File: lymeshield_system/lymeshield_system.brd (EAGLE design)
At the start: 67.9 x 49.5 mm, 56 parts, among them J1 TSW-106-16-L-S-RA, J2 M04B, J3 TSW-103-07-G-D-LL, J4 1844210, U1 MCP79410-I_SN, U2 ATMEGA1608-MU, U3 MX25V1635FM1I, U4 OPA2349EA, U5 DRV8838DSGR, U6 DRV5057A2QDBZ, U7 STLQ015M33R, Y1 ECS-.327-9-1210-TR, Y2 ECS-.327-9-1210-TR

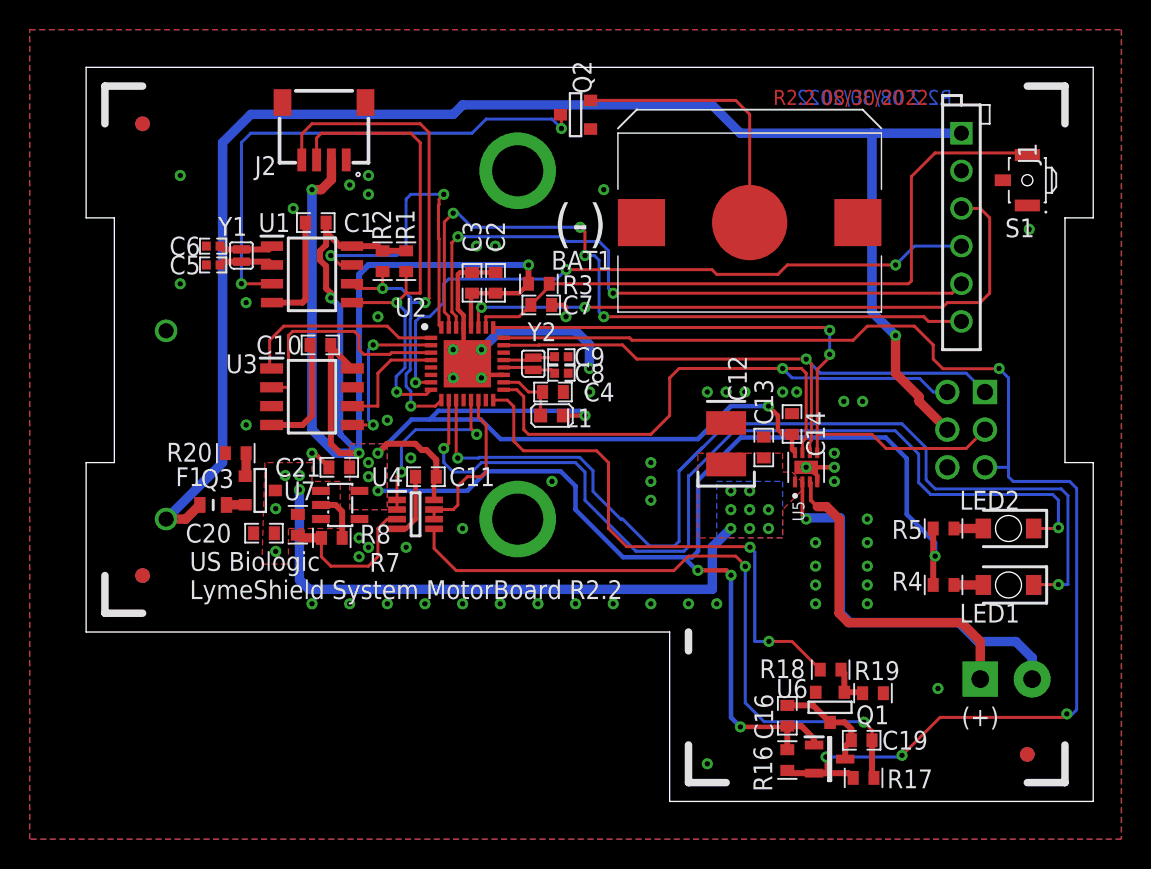
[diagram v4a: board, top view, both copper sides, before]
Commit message: fix (schematics/layout): update for 2.3.a build - Add variant "A" to schematics - Modify footprints for polarization - Update silkscreen for 2.3.a
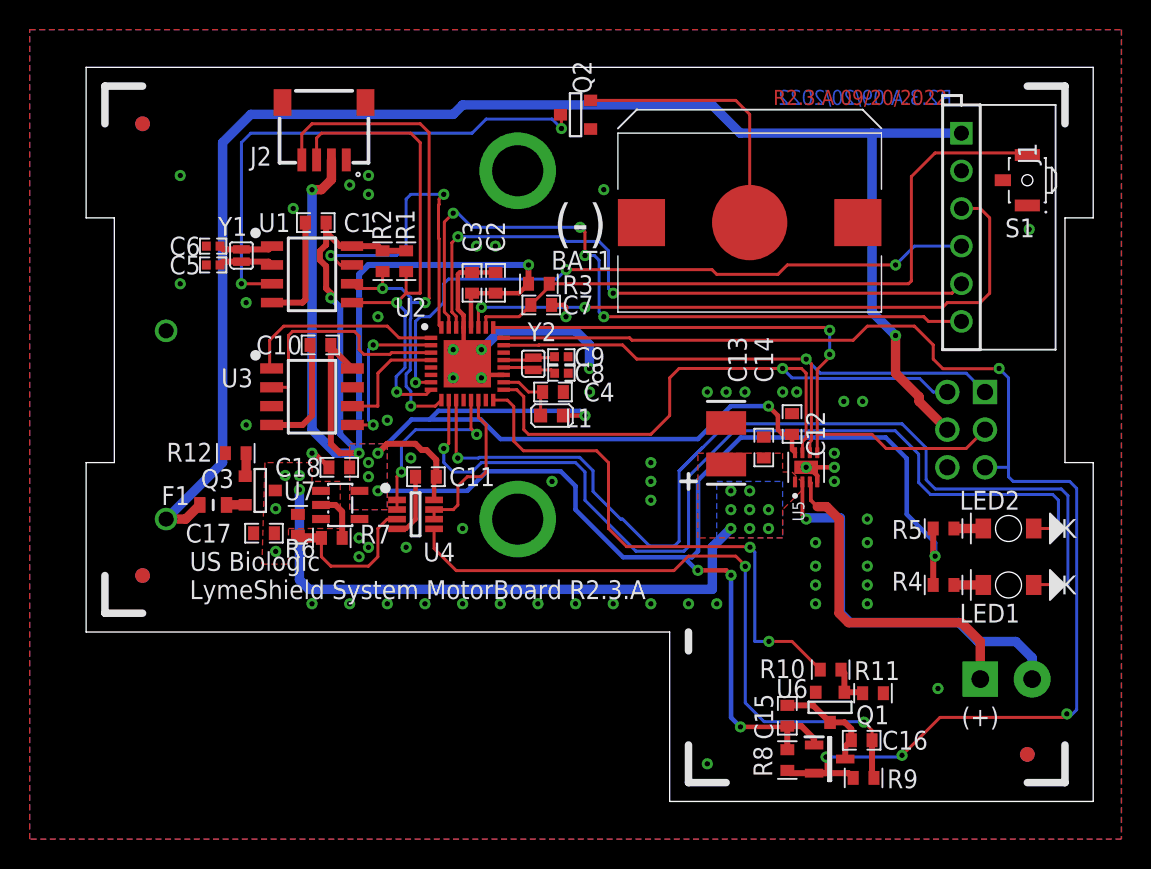
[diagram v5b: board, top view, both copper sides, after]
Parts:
- removed C19: 100nF, HatchPoint-Capacitors:CAPC_0603_1608X90N
- removed R16: 1.00K, HatchPoint-Resistors:R0603K
- added C15: 100nF, HatchPoint-Capacitors:CAPC_0603_1608X90N
- added R6: 1.20M, HatchPoint-Resistors:R0603K
- C12: value TAJB226M010RNJ -> 100nF; device HatchPoint-Capacitors:PCAPC_1210 -> HatchPoint-Capacitors:CAPC_0603_1608X90N
- C13: value 100nF -> TAJB226M010RNJ; device HatchPoint-Capacitors:CAPC_0603_1608X90N -> HatchPoint-Capacitors:PCAPC_1210
- R8: value 1.20M -> 1.00K
- moved R8 34.5 mm to (47.3, -7.94), turned to 270 degrees
- moved C16 5.79 mm to (53.0, -7.30), turned to 180 degrees
- moved C12 4.49 mm to (47.6, 13.3)
- moved C13 2.71 mm to (43.2, 12.7)
- moved C14 2.48 mm to (45.7, 11.7)
- moved R7 2.25 mm to (15.9, 6.35), turned to 0 degrees
- renumbered C20 to C17, C21 to C18, R17 to R9, R18 to R10, R19 to R11, R20 to R12
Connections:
- net DGND: now also R7.2; no longer R8.2
- net HALL_PWM_SENSE: now also R8.2; no longer R16.2
- net N$10: now also R6.2, R7.1; no longer R7.2, R8.1
- net N$20: now also C16.1; no longer C19.1
- net N$23: now also C15.2; no longer C19.2
- net VCC: now also C12.1, C15.1, R8.1; no longer C14.1, C16.1, R16.1
- net V_BAT: now also C14.1, R6.1; no longer C12.1, R7.1
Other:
- board text added: "R2.3.A 09/20/2022"
- board text added: "US Biologic LymeShield System MotorBoard R2.3.A"
- board text removed: "R2.2 08/30/2022"
- board text removed: "US Biologic LymeShield System MotorBoard R2.2"
